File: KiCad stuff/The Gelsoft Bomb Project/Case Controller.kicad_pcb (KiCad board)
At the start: 2 copper layers, 33 parts, among them J1 ISP, J2 Module Connector, J3 Battery Header, J4 Low-Power Switch, SW1 Power Switch, SW2 PLUS, SW3 MINUS, SW4 OK, U1 Buck_Converter_Module_7-26v, U1 TPS56339DDCR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

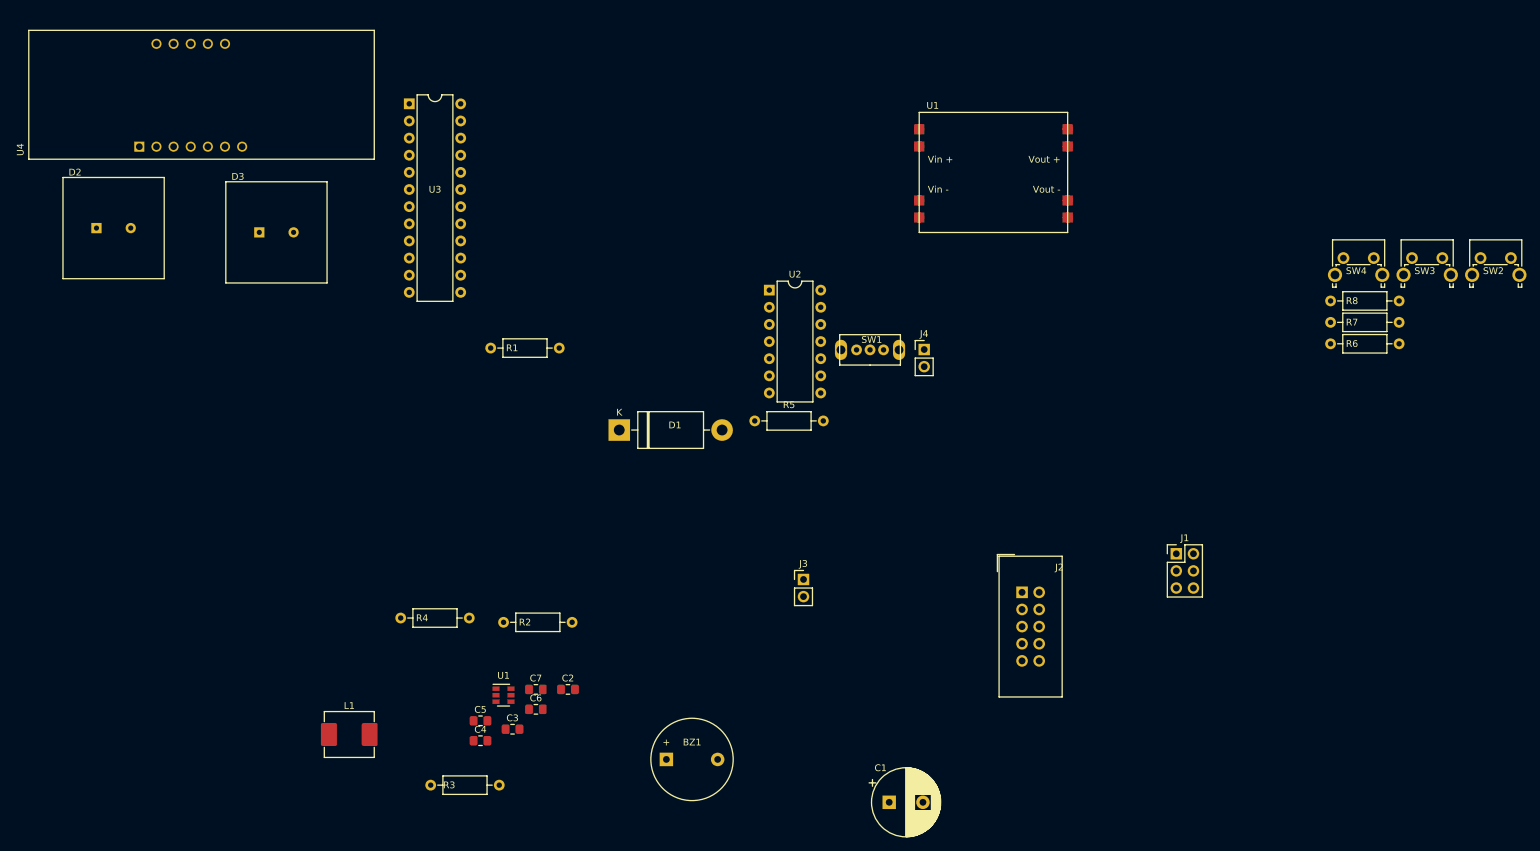
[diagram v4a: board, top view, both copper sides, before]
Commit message: Update footprints and use new layout
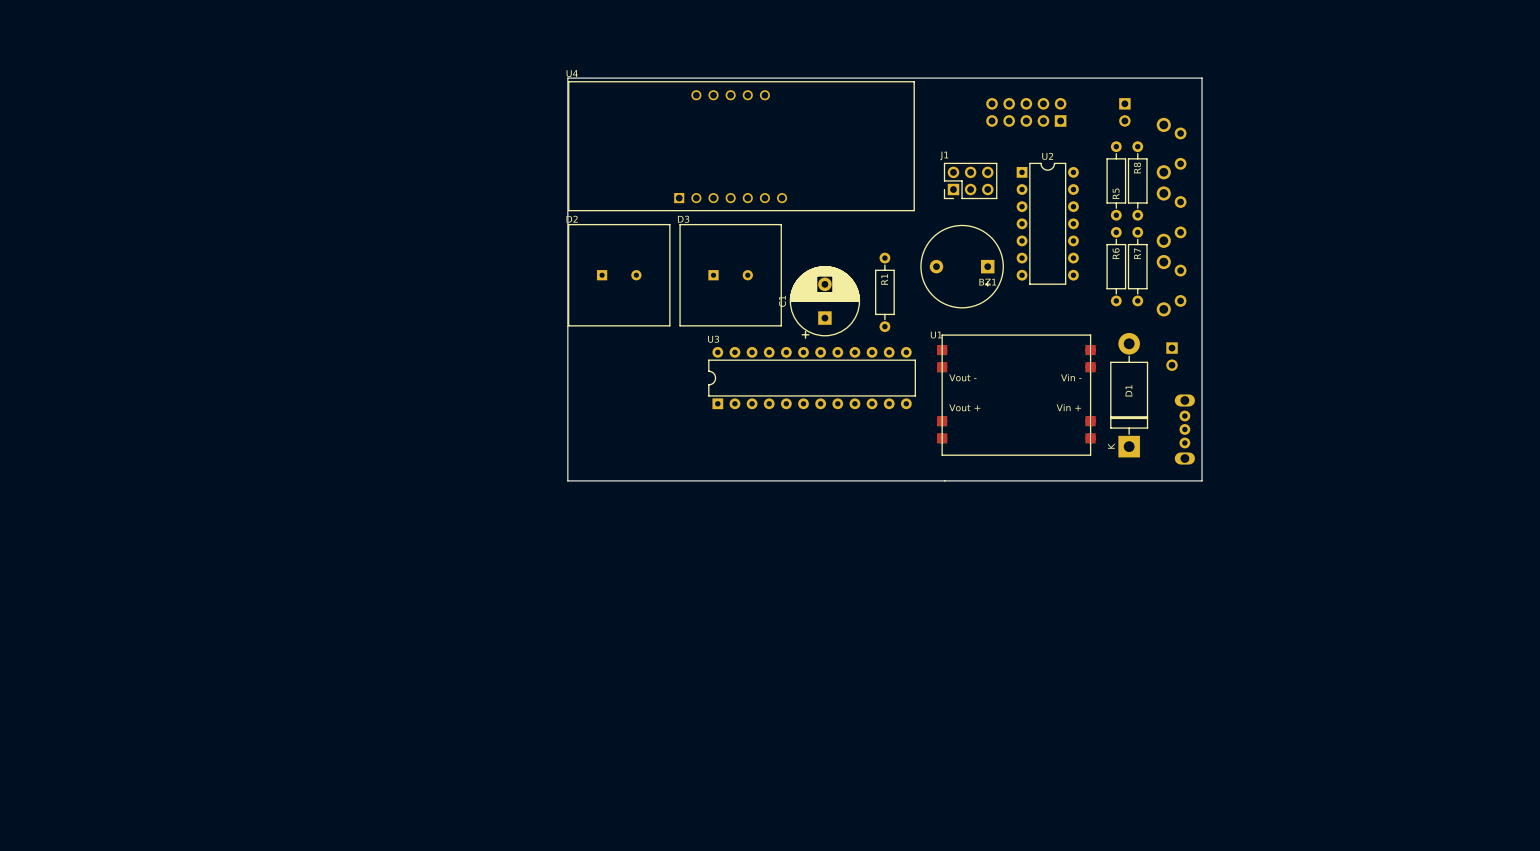
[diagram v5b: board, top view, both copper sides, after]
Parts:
- removed C2, C3: 10uF, Capacitor_SMD:C_0805_2012Metric_Pad1.15x1.40mm_HandSolder
- removed C4, C5: 0.1uF, Capacitor_SMD:C_0805_2012Metric_Pad1.15x1.40mm_HandSolder
- removed C6, C7: 22uF, Capacitor_SMD:C_0805_2012Metric_Pad1.15x1.40mm_HandSolder
- removed L1: 5.6uH, Inductor_SMD:L_Abracon_ASPI-0630LR
- removed R2: 30, Resistor_THT:R_Axial_DIN0207_L6.3mm_D2.5mm_P10.16mm_Horizontal
- removed R3: 52.3k, Resistor_THT:R_Axial_DIN0207_L6.3mm_D2.5mm_P10.16mm_Horizontal
- removed R4: 10k, Resistor_THT:R_Axial_DIN0207_L6.3mm_D2.5mm_P10.16mm_Horizontal
- removed the U1 at (151.1, 31.8)
- removed the U1 at (89.5, 118.1)
- added U1: Buck_Converter_Module_7-26v, The Gelsoft Bomb Project:Buck_Converter_Module_7-24v, F.Cu at (176.5, 82.5)
- J2, J3, J4, SW1, SW2, SW3, SW4: moved to B.Cu
- moved BZ1 87.2 mm to (161.3, 54.6), turned to 180 degrees
- moved U4 80.4 mm to (118.1, 44.5)
- moved D1 75.6 mm to (182.2, 81.3), turned to 90 degrees
- moved D2 72.7 mm to (104.1, 55.9)
- moved C1 72.4 mm to (137.2, 62.2), turned to 90 degrees
- moved J2 70.1 mm to (172.1, 33.0), turned to 90 degrees
- moved R5 67.2 mm to (180.3, 36.8), turned to 270 degrees
- moved D3 65.1 mm to (120.7, 55.9)
- moved J3 64.5 mm to (188.6, 66.7), turned to 180 degrees
- moved U3 63.8 mm to (121.3, 74.9), turned to 90 degrees
- moved J1 63.3 mm to (156.2, 43.2), turned to 90 degrees
- moved R1 58.5 mm to (146.1, 63.5), turned to 90 degrees
- moved SW1 48.1 mm to (190.5, 78.7), turned to 270 degrees
- moved J4 47.0 mm to (181.6, 30.5), turned to 180 degrees
- moved SW2 44.9 mm to (189.9, 59.7), turned to 90 degrees
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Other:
- board outline added: 94 x 59.7 mm

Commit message: Route PCB
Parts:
- moved J1 5.68 mm to (161.3, 40.6), turned to 270 degrees
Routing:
- net 5v: track 0.00 -> 153.8 mm
- net VIN: track 0.00 -> 82.8 mm, vias 0 -> 1
- net Net-(U2-Pad2): track 0.00 -> 62.6 mm
- net Net-(D2-Pad1): track 0.00 -> 60.4 mm
- net Net-(U3-Pad11): track 0.00 -> 55.5 mm, vias 0 -> 1
- net Net-(U3-Pad6): track 0.00 -> 53.2 mm
- net Net-(U3-Pad14): track 0.00 -> 52.6 mm
- net Net-(D3-Pad1): track 0.00 -> 49.1 mm, vias 0 -> 1
- net Net-(U3-Pad15): track 0.00 -> 46.8 mm
- net Net-(D2-Pad2): track 0.00 -> 42.6 mm
- net MISO: track 0.00 -> 37.2 mm, vias 0 -> 2
- net MOSI: track 0.00 -> 36.4 mm, vias 0 -> 1
- net Net-(U3-Pad21): track 0.00 -> 35.0 mm
- net SCK: track 0.00 -> 34.4 mm
- net Net-(U3-Pad17): track 0.00 -> 33.6 mm
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- added copper zone on B.Cu, net Earth
- added copper zone on F.Cu, net Earth
